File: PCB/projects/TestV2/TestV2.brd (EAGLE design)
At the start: 100 x 100 mm, 109 parts, among them Q1 35A/25V/8.5mΩ, Q2 5.8A/30V/35mΩ, Q3 60V/32A/35mΩ, X1 USB-MINIB

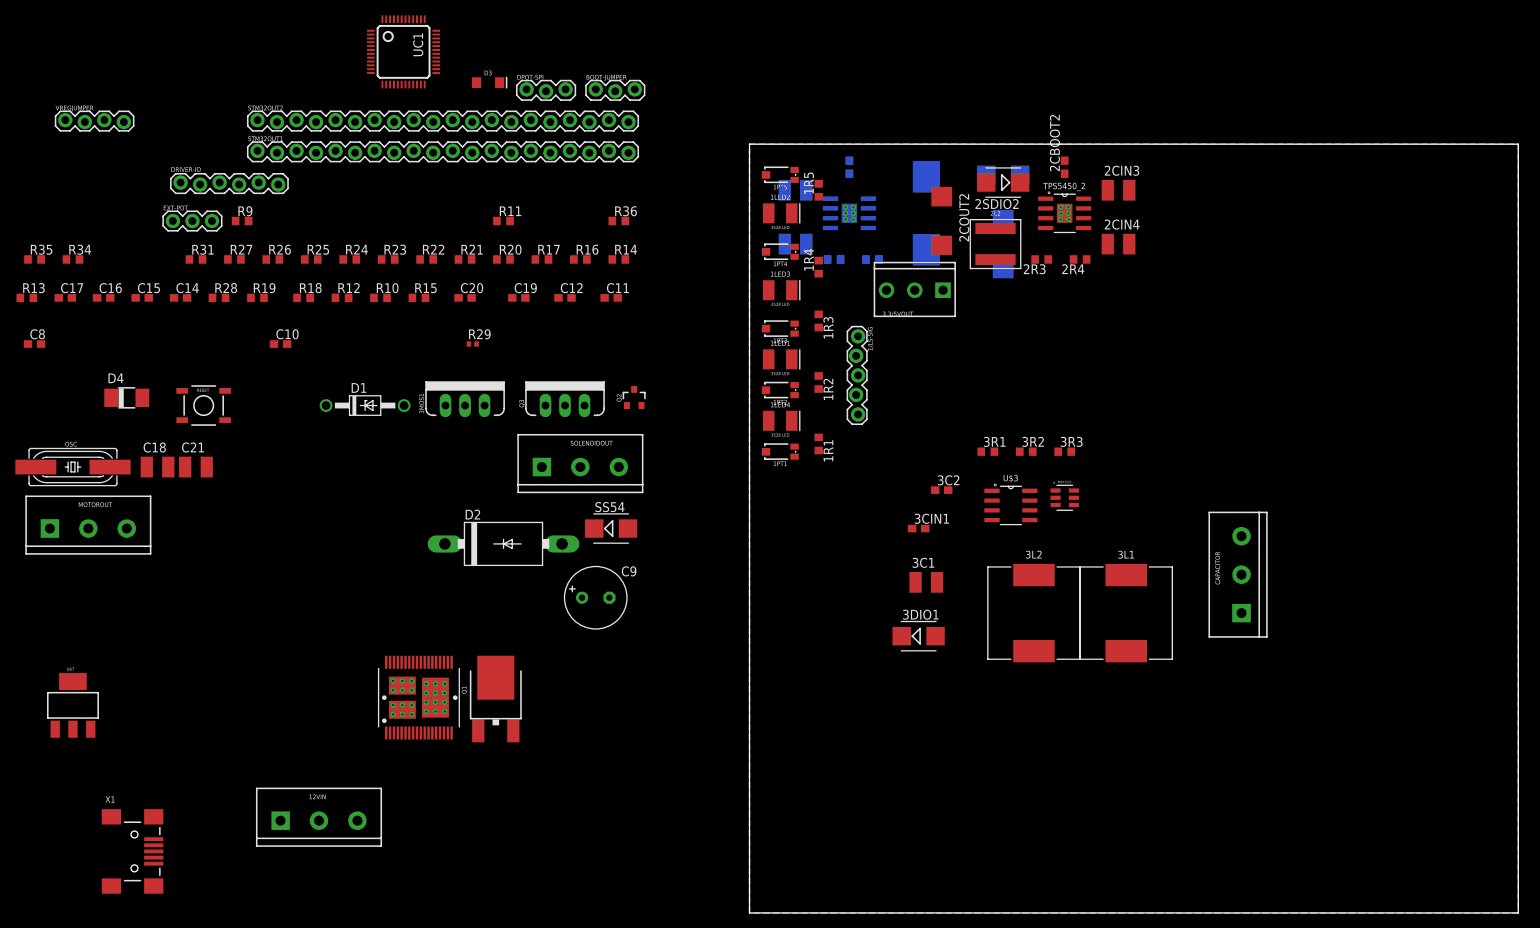
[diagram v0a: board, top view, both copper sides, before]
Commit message: 8/12 PCB well well well so drunk the original commit name was 9/12 renamed all parts in schematic, then everything went downhill welp was in 1mm grid instead of 1.27mm forgot to check drc before routing and placing everything, will redo all the placements soon lesson: dont be stupid thanks the upside is we may actually have a very legit motor driver and new pill module rip
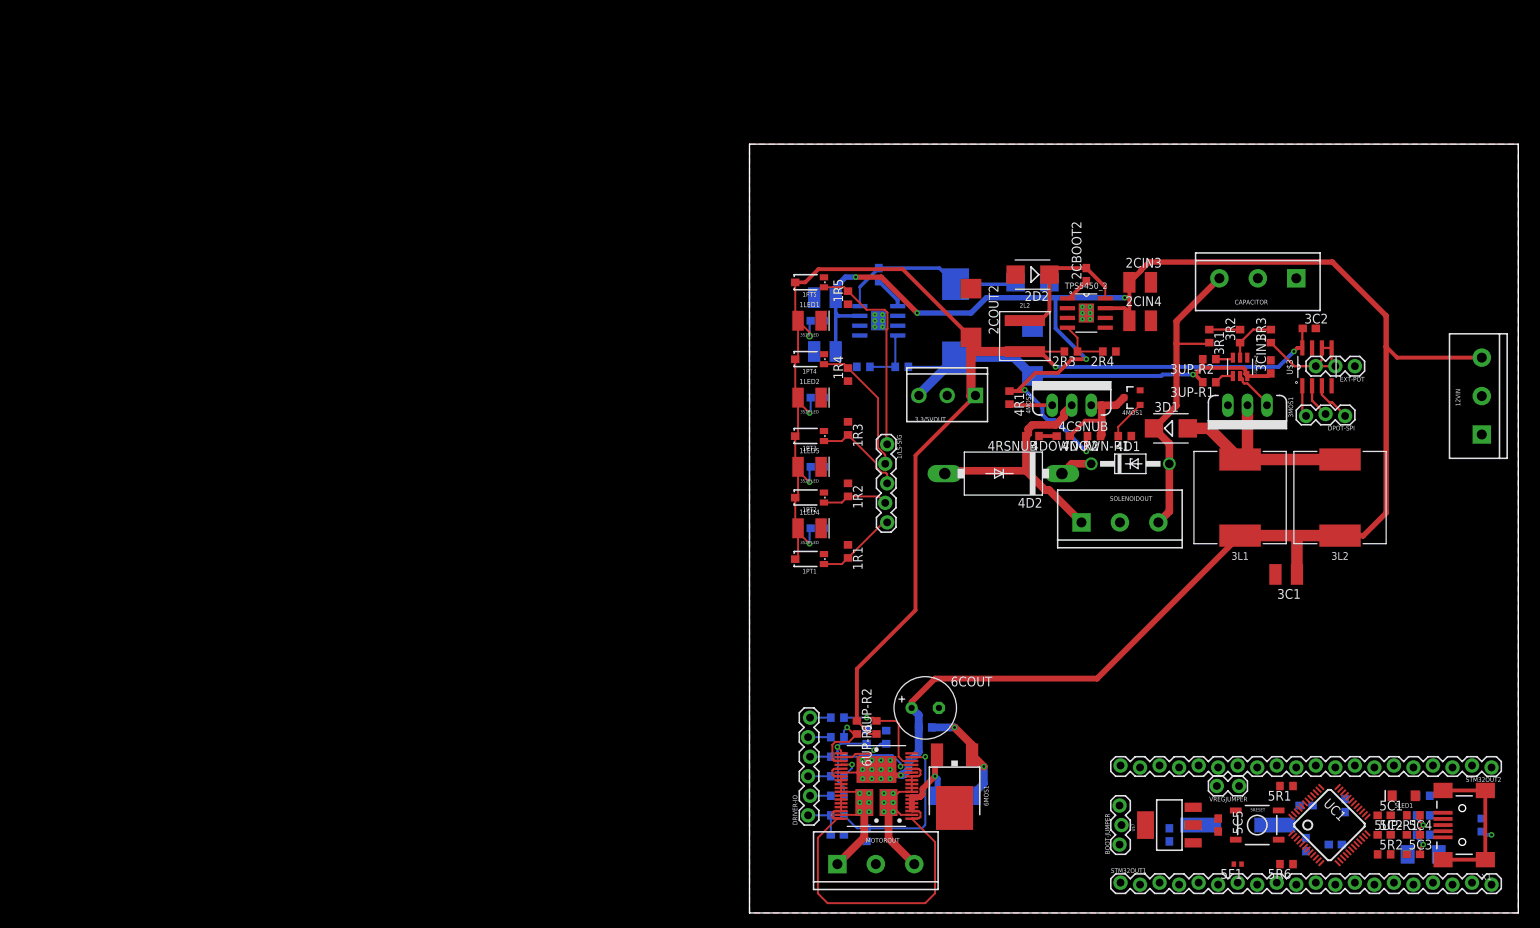
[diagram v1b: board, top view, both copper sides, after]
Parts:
- removed 1LED3: 3528LED, JH:3528
- removed 2SDIO1, 2SDIO2: SS54, diode:SMB
- removed 3DIO1: SS510, diode:SMB
- removed C10: 1500pF, rcl:C0603
- removed C11, C12: 47pF, rcl:C0603
- removed C14, C15, C16, C17: 1uF, rcl:C0603
- removed C18: 22uf, rcl:C1210
- removed C19, C20: 18pF, rcl:C0603
- removed C21: 22uF, rcl:C1210
- removed C8: 33nF, rcl:C0603
- removed C9: 680uF/16V, rcl:E3,5-8
- removed D1: 1N4728, diode:DO41Z10
- removed D2: 1N5401, diode:DO201-15
- removed D3: RED, SparkFun-LED:LED-1206
- removed D4: SS14, diode:DO-214AC
- removed OSC: 8MHz, SparkFun-Clocks:HC49UP
- removed Q1: 35A/25V/8.5mΩ, SparkFun-DiscreteSemi:DPAK
- removed Q2: 5.8A/30V/35mΩ, SparkFun-DiscreteSemi:SOT23-3
- removed Q3: 60V/32A/35mΩ, SparkFun-DiscreteSemi:TO220V
- removed R10, R12, R19: 4.7k, rcl:R0603
- removed R11, R13, R14, R16, R23, R25, R36, R9: 1k, rcl:R0603
- removed R15: 100k, rcl:R0603
- removed R17, R20, R21, R22, R34, R35: 10k, rcl:R0603
- removed R18, R28: 1.5k, rcl:R0603
- removed R24: 20, rcl:R0603
- removed R26, R27, R31: 22, rcl:R0603
- removed R29: 300ohm bead, rcl:R0402
- removed RESET: TAC_SWITCHSMD, SparkFun-Retired:TACTILE-SWITCH-SMD
- removed SS54: 5A/40V, diode:SMB
- added 1C1, 1C2, 1C3, 1C4, 5C10, 5C5, 5C7, 5C8, 5C9: 1uF, rcl:C0603
- added 1LED5: 3528LED, JH:3528
- added 2D1, 2D2: SS54, diode:SMB
- added 3D1: SS510, diode:SMB
- added 3UP-R1, 3UP-R2, 4R1, 5R1, 5R5, 6R1, 6R2, 6R3, 6R4, 6R5: 1k, rcl:R0603
- added 4CSNUB: 1500pF, rcl:C0603
- added 4D1: 1N4728, diode:DO41Z10
- added 4D2: 1N5401, diode:DO201-15
- added 4DOWN-R1, 4DOWN-R2, 5R2, 5R6, 6DOWN-R3, 6R6: 10k, rcl:R0603
- added 4MOS1: AO3400, SparkFun-DiscreteSemi:SOT23-3
- added 4MOS2: STP75NF75, SparkFun-DiscreteSemi:TO220V
- added 4RSNUB: 20, rcl:R0603
- added 5C1, 5C2: 18pF, rcl:C0603
- added 5C3, 5C4: 47pF, rcl:C0603
- added 5C6: 1uf, rcl:C0603
- added 5D1: SS14, diode:DO-214AC
- added 5DOWN-R1, 5R3, 5R4: 22, rcl:R0603
- added 5F1: 300ohm bead, rcl:R0402
- added 5LED1: RED, SparkFun-LED:LED-1206
- added 5OSC: 8MHz, SparkFun-Clocks:HC49UP
- added 5RESET: TAC_SWITCHSMD, SparkFun-Retired:TACTILE-SWITCH-SMD
- added 5UP-R1, 6DOWN-R1: 1.5k, rcl:R0603
- added 6C1: 33nF, rcl:C0603
- added 6COUT: 680uF/16V, rcl:E3,5-8
- added 6D1: 5A/40V, diode:SMB
- added 6DOWN-R2, 6UP-R1, 6UP-R2: 4.7k, rcl:R0603
- added 6MOS1: AP86T02GH, SparkFun-DiscreteSemi:DPAK
- added 6R7: 100k, rcl:R0603
- VREGJUMPER: device SparkFun-Connectors:1X04_LOCK -> SparkFun-Connectors:1X02_LOCK
- moved STM32OUT2 181.1 mm to (96.5, 19.1), turned to 180 degrees
- moved VREGJUMPER 175.3 mm to (63.5, 16.5), turned to 180 degrees
- moved X1 172.7 mm to (92.7, 11.4), turned to 180 degrees
- moved 12VIN 164.1 mm to (95.2, 62.2), turned to 90 degrees
- moved UC1 156.9 mm to (75.4, 11.4), turned to 315 degrees
- moved EXT-POT 154.9 mm to (78.7, 71.1), turned to 180 degrees
- moved STM32OUT1 147.2 mm to (48.3, 3.81)
- moved U$7 143.5 mm to (54.6, 11.4), turned to 90 degrees
- moved BOOT-JUMPER 119.5 mm to (48.3, 8.89), turned to 90 degrees
- moved DRIVER-IO 115.9 mm to (7.62, 12.7), turned to 90 degrees
- moved DPOT-SPI 114.5 mm to (77.5, 64.8), turned to 180 degrees
- moved MOTOROUT 111.3 mm to (11.4, 6.35)
- moved 3MOS1 101.8 mm to (64.8, 66.0), turned to 180 degrees
- moved SOLENOIDOUT 70.5 mm to (43.2, 50.8)
- moved U$6 60.6 mm to (16.5, 16.5), turned to 90 degrees
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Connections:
- removed net 33: R25.2, UC1.19
- removed net N$41: U$7.2, VREGJUMPER.3
- removed net OUT_A: MOTOROUT.1, U$6.2, U$6.P$10, U$6.P$11, U$6.P$12, U$6.P$7, U$6.P$8, U$6.P$9, U$6.P10, U$6.P11, U$6.P12, U$6.P14, U$6.P2, U$6.P8, U$6.P9
- removed net OUT_B: MOTOROUT.3, U$6.3, U$6.P$1, U$6.P$2, U$6.P$3, U$6.P$4, U$6.P$5, U$6.P$6, U$6.P23, U$6.P25, U$6.P26, U$6.P27, U$6.P28, U$6.P29, U$6.P35
- new net N$25: 3UP-R1.1, MAX1522.4
- new net N$29: 3UP-R2.1, MAX1522.3
- new net N$31: 5R5.2, UC1.19
- new net N$32: MOTOROUT.3, U$6.2, U$6.P$10, U$6.P$11, U$6.P$12, U$6.P$7, U$6.P$8, U$6.P$9, U$6.P10, U$6.P11, U$6.P12, U$6.P14, U$6.P2, U$6.P8, U$6.P9
- new net N$33: MOTOROUT.1, U$6.3, U$6.P$1, U$6.P$2, U$6.P$3, U$6.P$4, U$6.P$5, U$6.P$6, U$6.P23, U$6.P25, U$6.P26, U$6.P27, U$6.P28, U$6.P29, U$6.P35
- net 0: now also STM32OUT1.20; no longer STM32OUT1.19
- net 1: now also STM32OUT1.19; no longer STM32OUT1.18
- net 12V: now also 4DOWN-R2.2, 4R1.1, 6COUT.+, 6R7.1; no longer C9.+, R15.1, R22.2, R23.1
- net 2: now also STM32OUT1.18; no longer STM32OUT1.17
- net 23_USBDP: now also 5C4.2, 5R4.1, 5UP-R1.1; no longer C12.2, R27.1, R28.1
- net 24_USBDM: now also 5C3.2, 5R3.1; no longer C11.2, R26.1
- net 3.3V: now also 1C1.1, 1C2.1, 1C3.1, 1C4.1, 1LED5.A, 5C10.1, 5C6.1, 5C7.1, 5C8.1, 5C9.1, 5R2.2, 5UP-R1.2, 6UP-R1.1, 6UP-R2.1, U$7.2; no longer 1LED3.A, C14.1, C15.1, C16.1, C17.1, C18.1, R10.1, R12.1, R28.2, R35.2, VREGJUMPER.4
- net 32: now also 5R6.1; no longer R34.1
- net 5V: now also 3UP-R1.2, 3UP-R2.2, 5C5.1, 5D1.C; no longer C21.1, D4.C, MAX1522.3, MAX1522.4
- net AGND: now also 5C10.2, 5F1.1, STM32OUT1.7; no longer C14.2, R29.1
- net CS: now also 6R5.2; no longer R16.2
- net EN_A: now also 6R1.2; no longer R9.2
- net EN_B: now also 6R2.1; no longer R11.1
- net GND: now also 1C1.2, 1C2.2, 1C3.2, 1C4.2, 1LED5.C, 2D1.A, 2D2.A, 4DOWN-R1.1, 4MOS1.2, 5C1.2, 5C2.2, 5C3.1, 5C4.1, 5C5.2, 5C6.2, 5C7.2, 5C8.2, 5C9.2, 5DOWN-R1.1, 5F1.2, 5LED1.C, 5R1.1, 6C1.2, 6COUT.-, 6DOWN-R1.2, 6DOWN-R2.2, 6DOWN-R3.2, 6MOS1.4; no longer 1LED3.C, 2SDIO1.A, 2SDIO2.A, C11.1, C12.1, C15.2, C16.2, C17.2, C18.2, C19.2, C20.2, C21.2, C8.2, C9.-, D3.C, Q1.4, Q2.2, R18.2, R19.2, R20.2, R21.1, R29.2, R31.1, R36.1
- net IN_A: now also 6R3.2; no longer R14.2
- net IN_B: now also 6R4.1; no longer R13.1
- net N$1: now also 2D1.C; no longer 2SDIO1.C
- net N$11: now also 3D1.A; no longer 3DIO1.A
- net N$12: now also 6R1.1, 6UP-R2.2; no longer R10.2, R9.1
- net N$13: now also 6R3.1; no longer R14.1
- net N$14: now also 6R2.2, 6UP-R1.2; no longer R11.2, R12.2
- net N$15: now also 6R4.2; no longer R13.2
- net N$16: now also 6DOWN-R2.1, 6R6.2; no longer R17.2, R19.1
- net N$17: now also 6DOWN-R1.1, 6R5.1; no longer R16.1, R18.1
- net N$19: now also 6D1.A, 6MOS1.3; no longer Q1.3, SS54.A
- net N$20: now also 6D1.C, 6MOS1.1, 6R7.2; no longer Q1.1, R15.2, SS54.C
- net N$21: now also 6DOWN-R3.1; no longer R20.1
- net N$22: now also 4CSNUB.2, 4DOWN-R2.1, 4MOS1.3, 4MOS2.3; no longer C10.2, Q2.3, Q3.3, R22.1
- net N$23: now also 4MOS2.1, 4R1.2; no longer Q3.1, R23.2
- net N$24: now also 4D1.C, 4D2.C; no longer D1.C, D2.C
- net N$26: now also 4CSNUB.1, 4RSNUB.1; no longer C10.1, R24.1
- net N$27: now also 5R1.2, 5RESET.1, 5RESET.2; no longer R36.2, RESET.1, RESET.2
- net N$28: now also 5LED1.A, 5R5.1; no longer D3.A, R25.1
- net N$30: now also 5R6.2; no longer R34.2
- net N$36: now also 5DOWN-R1.2; no longer R31.2
- net N$5: now also 2D2.C; no longer 2SDIO2.C
- net N$59: now also 5R3.2; no longer R26.2
- net N$60: now also 5R4.2; no longer R27.2
- net OSC_IN: now also 5C2.1, 5OSC.2; no longer C19.1, OSC.2
- net OSC_OUT: now also 5C1.1, 5OSC.1; no longer C20.1, OSC.1
- net PWM: now also 6C1.1, 6R6.1; no longer C8.1, R17.1
- net RESET: now also 5R2.1, 5RESET.3, 5RESET.4; no longer R35.1, RESET.3, RESET.4, STM32OUT1.7
- net SOLENOID-: now also 4D2.A, 4MOS2.2, 4RSNUB.2, SOLENOIDOUT.1; no longer D2.A, Q3.2, R24.2, SOLENOIDOUT.3
- net SOLENOIDON: now also 4DOWN-R1.2, 4MOS1.1; no longer Q2.1, R21.2, STM32OUT1.20
- net VCC_1: now also 3D1.C, 4D1.A, SOLENOIDOUT.3; no longer 3DIO1.C, D1.A, SOLENOIDOUT.1
- net V_USB: now also 5D1.A; no longer D4.A
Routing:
- net 12V: track 0.00 -> 286.8 mm, vias 0 -> 7
- net 3.3V: track 0.00 -> 195.2 mm, vias 0 -> 6
- net 5V: track 0.00 -> 58.4 mm, vias 0 -> 1
- net N$19: track 0.00 -> 57.9 mm, vias 0 -> 1
- net VCC_1: track 0.00 -> 41.0 mm
- net SOLENOID-: track 0.00 -> 33.5 mm
- net N$11: track 0.00 -> 28.9 mm
- net N$32: track 0.00 -> 28.7 mm
- net N$68: track 0.00 -> 26.8 mm
- net N$33: track 0.00 -> 26.0 mm
- net N$1: track 0.00 -> 24.7 mm
- net N$16: track 0.00 -> 22.1 mm, vias 0 -> 1
- net N$36: track 0.00 -> 21.4 mm, vias 0 -> 1
- net N$5: track 0.00 -> 18.6 mm
- net N$67: track 0.00 -> 17.8 mm
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
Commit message: 11/12 PCB Updated own DRU file Updated even more stuff in schematic but quite minor, mostly flipping the 5mm screw terminal connections redid the pcb kinda redid the layout and managed to frkin manual route the stm32 new pill with 10mil traces oyas feelsgood super behind time again but lifes good
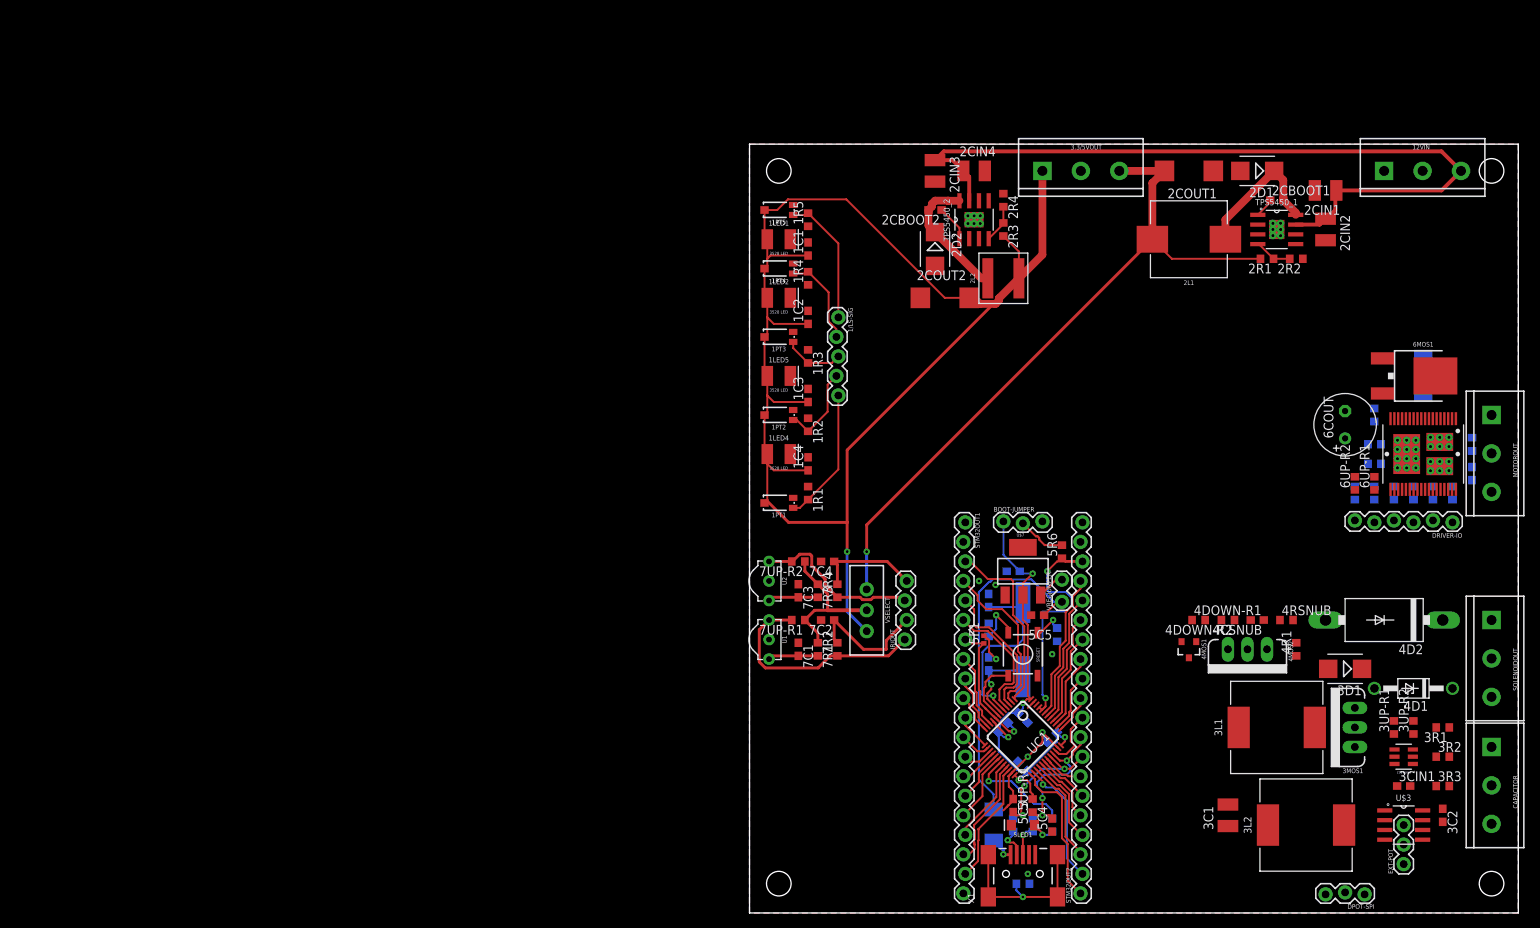
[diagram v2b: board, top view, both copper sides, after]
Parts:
- added 7C1, 7C3: 47uF, rcl:C0603
- added 7C2, 7C4: 1uF, rcl:C0603
- added 7R1, 7R3: (no value), rcl:R0603
- added 7R2, 7R4: 100k, rcl:R0603
- added 7UP-R1, 7UP-R2: 10k, rcl:R0603
- added IR/OUT: (no value), SparkFun-Connectors:1X04_LOCK
- added U1, U2: 38kHz, SparkFun-Sensors:TSOP382
- added VSELECT: (no value), SparkFun-Switches:SWITCH_SPDT_PTH_11.6X4.0MM_LOCK
- 3.3/5VOUT: device SparkFun-Connectors:SCREWTERMINAL-3.5MM-3_LOCK.007S -> SparkFun-Connectors:SCREWTERMINAL-5MM-3
- moved MOTOROUT 103.2 mm to (96.5, 64.8), turned to 270 degrees
- moved 6C1 95.0 mm to (94.0, 57.1), turned to 90 degrees
- moved 6DOWN-R2 93.7 mm to (94.0, 61.0)
- moved DRIVER-IO 92.1 mm to (91.4, 50.8), turned to 180 degrees
- moved 6R6 90.3 mm to (91.4, 54.6), turned to 90 degrees
- moved 6R5 86.9 mm to (88.9, 54.6), turned to 270 degrees
- moved 6R4 83.5 mm to (86.4, 54.6), turned to 90 degrees
- moved U$6 83.2 mm to (87.6, 59.7), turned to 180 degrees
- moved 6D1 81.8 mm to (87.6, 69.8), turned to 270 degrees
- moved 6MOS1 81.8 mm to (87.6, 69.8), turned to 270 degrees
- moved 6R3 80.1 mm to (83.8, 54.6), turned to 270 degrees
- moved 6R2 76.7 mm to (81.3, 54.6), turned to 90 degrees
- moved 6DOWN-R1 75.0 mm to (81.3, 58.4), turned to 0 degrees
- moved 6UP-R1 74.4 mm to (81.3, 55.9), turned to 90 degrees
- moved 6DOWN-R3 74.1 mm to (81.3, 61.0), turned to 0 degrees
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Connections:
- new net IR1RAW: 7R2.1, 7UP-R1.2, IR/OUT.1, U1.1
- new net IR2RAW: 7R4.1, 7UP-R2.2, IR/OUT.3, U2.1
- new net N$34: 7C1.2, 7R1.2, U1.3
- new net N$35: 7R1.1, 7R3.1, 7UP-R1.1, 7UP-R2.1, VSELECT.2
- new net N$41: 7C2.1, 7R2.2, IR/OUT.2
- new net N$43: 7C3.2, 7R3.2, U2.3
- new net N$44: 7C4.1, 7R4.2, IR/OUT.4
- net 0: now also STM32OUT1.19; no longer STM32OUT1.20
- net 1: now also STM32OUT1.18; no longer STM32OUT1.19
- net 2: now also STM32OUT1.17; no longer STM32OUT1.18
- net 3.3V: now also VSELECT.1
- net 5V: now also VSELECT.3
- net GND: now also 7C1.1, 7C2.2, 7C3.1, 7C4.2, CAPACITOR.3, U1.2, U2.2; no longer CAPACITOR.1
- net N$32: now also MOTOROUT.1; no longer MOTOROUT.3
- net N$33: now also MOTOROUT.3; no longer MOTOROUT.1
- net VCC_1: now also CAPACITOR.1; no longer CAPACITOR.3
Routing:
- net 12V: track 286.8 -> 104.2 mm, vias 7 -> 0
- net 5V: track 58.4 -> 136.3 mm
- net N$19: track 57.9 -> 0.00 mm, vias 1 -> 0
- net 3.3V: track 195.2 -> 249.0 mm
- net VCC_1: track 41.0 -> 0.00 mm
- net SOLENOID-: track 33.5 -> 0.00 mm
- net 32: track 0.00 -> 32.8 mm, vias 0 -> 2
- net IR1RAW: track 0.00 -> 29.7 mm
- net N$11: track 28.9 -> 0.00 mm
- net N$32: track 28.7 -> 0.00 mm
- net N$33: track 26.0 -> 0.00 mm
- net OSC_IN: track 0.00 -> 24.8 mm, vias 0 -> 1
- net VBAT: track 0.00 -> 23.7 mm
- net GND: track 0.00 -> 22.7 mm, vias 0 -> 7
- net N$16: track 22.1 -> 0.00 mm, vias 1 -> 0
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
